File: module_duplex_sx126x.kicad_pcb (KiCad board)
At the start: 4 copper layers, 55.4 x 49.3 mm, 38 parts, among them J1 USB_B_Mini, J2 Conn_01x06_Pin, J3 Conn_01x05, J4 Conn_01x04, J5 Conn_01x02_Pin, J6 Conn_01x02, SW1 SW_Push, U1 STM32F103C8Tx, U2 AMS1117-3.3, U3 SN65HVD230, U4 Ai-Thinker-Ra-02, U5 Ai-Thinker-Ra-02, Y1 16M, Y2 32.768k

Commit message: First Pass of full layout
Signed-off-by: Leonardo Celente <leocelente@gmail.com>
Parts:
- moved C2 1.65 mm to (97.6, 58.1), turned to 180 degrees
- moved C3 1.48 mm to (97.6, 56.5), turned to 180 degrees
- moved R5 0.14 mm to (68.2, 58.5)
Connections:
- J1 pad 6: unconnected-(J1-Shield-Pad6) -> GND
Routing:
- net GND: track 9.85 -> 398.6 mm, vias 0 -> 76
- net VCC: track 0.00 -> 82.0 mm, vias 0 -> 19
- net /SELECT: track 0.00 -> 30.7 mm, vias 0 -> 1
- net /PWM_1: track 0.00 -> 22.2 mm, vias 0 -> 1
- net /PWM_2: track 0.00 -> 20.0 mm, vias 0 -> 1
- net /NRST: track 20.3 -> 40.1 mm, vias 0 -> 2
- net /LSE_OUT: track 0.00 -> 18.5 mm
- net /I2C_SCL: track 0.00 -> 17.8 mm, vias 0 -> 1
- net /SWDIO: track 0.00 -> 17.7 mm, vias 0 -> 1
- net /SEND_LED: track 0.00 -> 17.5 mm, vias 0 -> 2
- net /I2C_SDA: track 0.00 -> 16.3 mm, vias 0 -> 1
- net /SWDCLK: track 0.00 -> 15.8 mm, vias 0 -> 1
- net /RECV_LED: track 0.00 -> 14.4 mm, vias 0 -> 2
- net /LSE_IN: track 0.00 -> 14.0 mm
- net /HSE_OUT: track 0.56 -> 12.3 mm
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- added copper zone on F.Cu, net GND
- added copper zone on In1.Cu, net GND
- added copper zone on F.Cu, net VBUS
- added copper zone on F.Cu, net VCC
- added copper zone on In2.Cu, net VCC
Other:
- board text added: "RADIO_RECV"
- board text added: "RADIO_SEND"
- board text added: "SCK"
- board text added: "SEL"
- board text removed: "CLK"
- board text removed: "RADIO RX"
- board text removed: "RADIO TX"
- board text removed: "SELECT CAN"

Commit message: Added LCSC part numbers for production
Signed-off-by: Leonardo Celente <leocelente@gmail.com>
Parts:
- C4, C5: value 7p -> 6p
- C6, C7: value 24p -> 22p

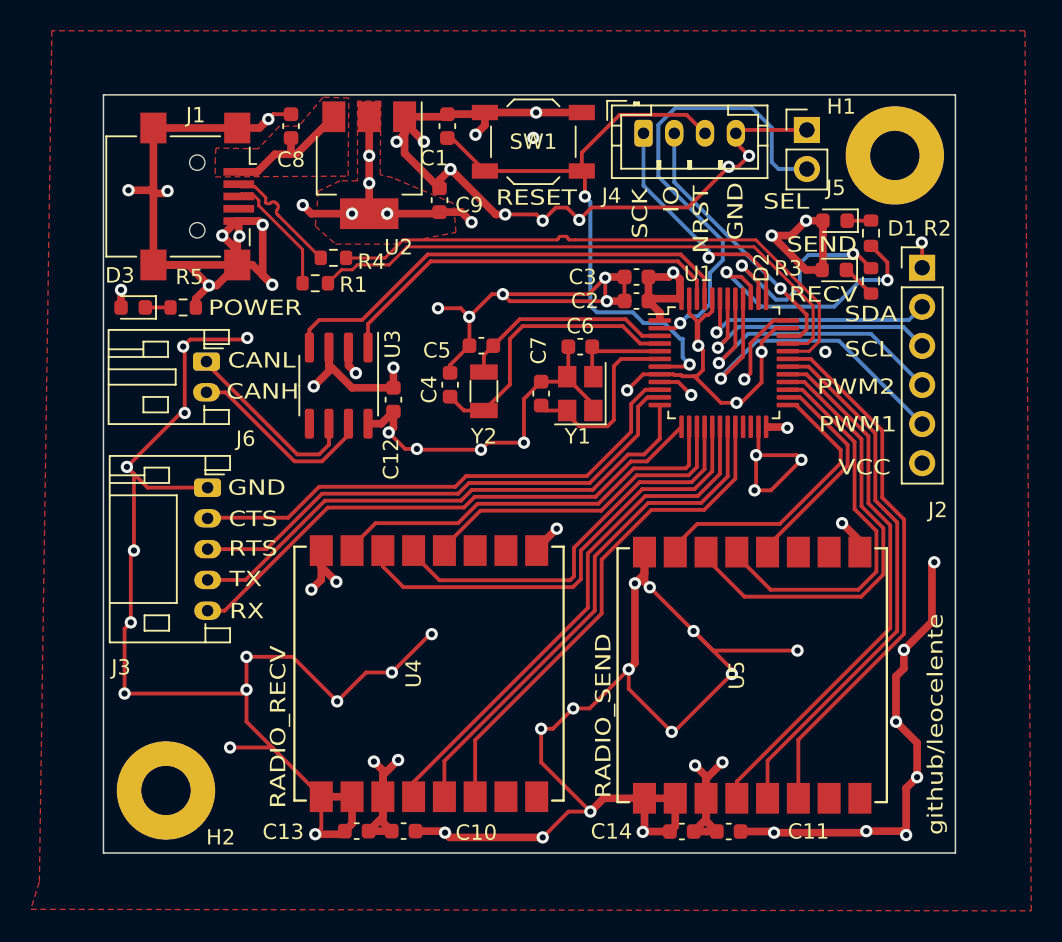
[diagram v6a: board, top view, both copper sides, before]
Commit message: Minor tweaks to vias
Signed-off-by: Leonardo Celente <leocelente@gmail.com>
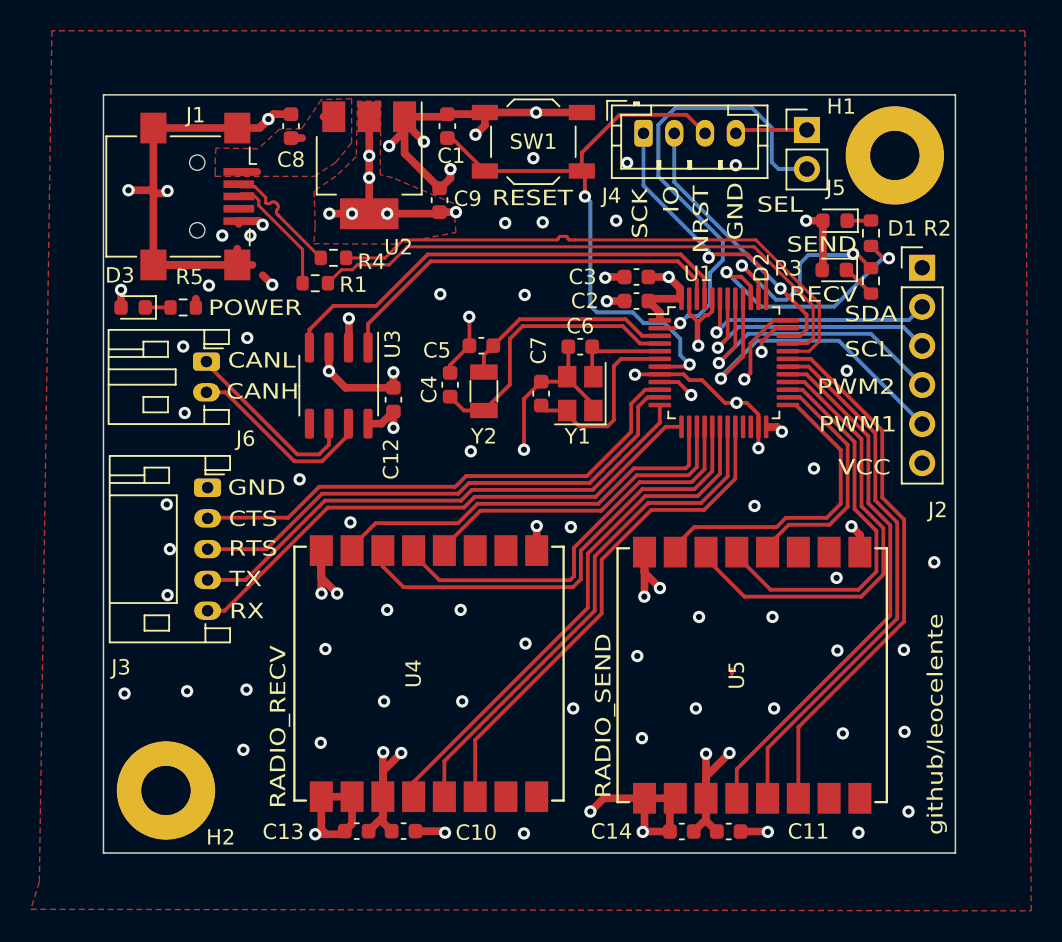
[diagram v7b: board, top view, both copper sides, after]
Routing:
- net GND: track 398.6 -> 160.4 mm, vias 76 -> 83
- net VCC: track 82.0 -> 65.5 mm, vias 19 -> 18
- net VBUS: track 8.71 -> 2.59 mm
- net /RADIO_SEND_NSS: track 18.9 -> 20.4 mm
- net /RADIO_SEND_SCK: track 14.3 -> 15.8 mm
- net /UART_TX: track 35.4 -> 34.8 mm

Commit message: Changed connector to jumper; Added USB DM pullup
Signed-off-by: Leonardo Celente <leocelente@gmail.com>
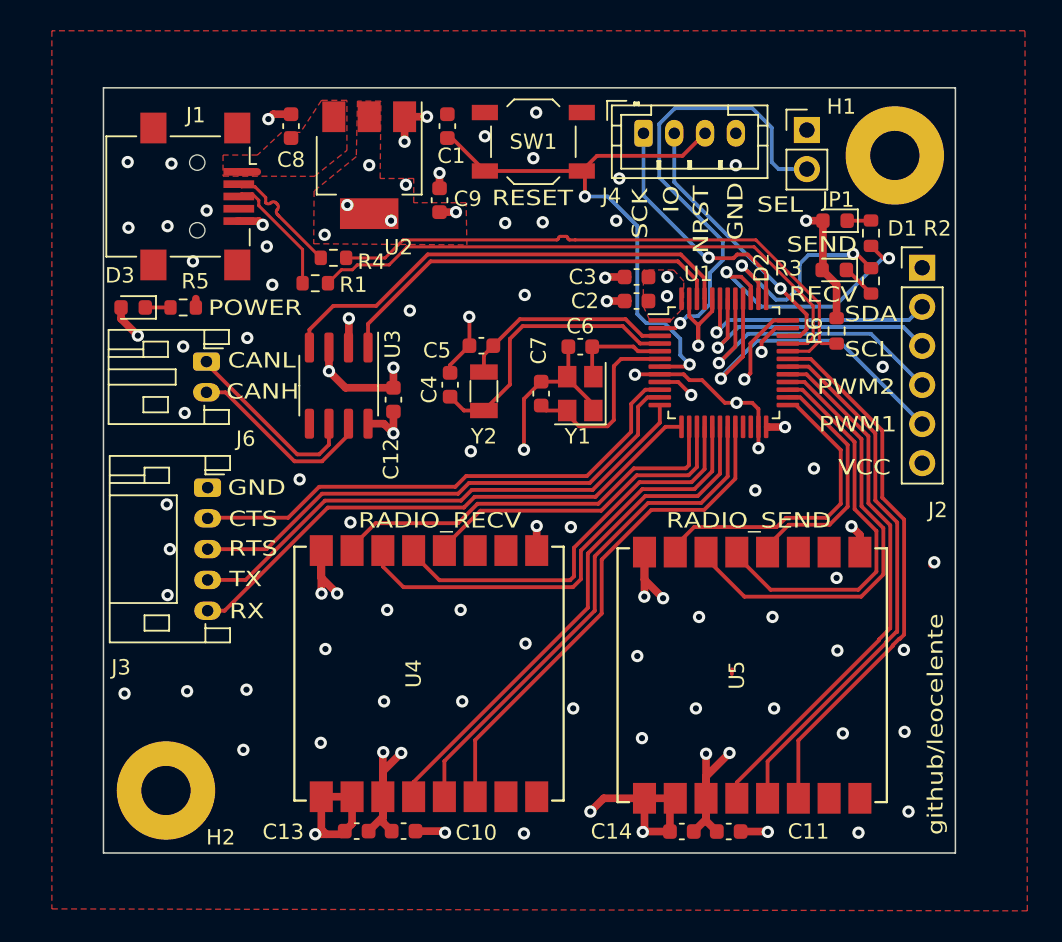
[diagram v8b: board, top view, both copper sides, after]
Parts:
- removed J5: Conn_01x02_Pin, Connector_PinHeader_2.54mm:PinHeader_1x02_P2.54mm_Vertical
- added JP1: Jumper_2_Open, Connector_PinHeader_2.54mm:PinHeader_1x02_P2.54mm_Vertical, F.Cu at (108.7, 47.0)
- added R6: 1.5k, Resistor_SMD:R_0603_1608Metric, F.Cu at (110.6, 60.0)
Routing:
- net GND: track 160.4 -> 101.1 mm, vias 83 -> 85
- net VCC: track 65.5 -> 50.8 mm, vias 18 -> 19
- net /NRST: track 40.0 -> 37.7 mm
- net VBUS: track 2.59 -> 1.20 mm
- net /USB_DN: track 38.0 -> 39.2 mm
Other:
- board size 55.4 x 49.3 mm -> 55.4 x 49.7 mm
